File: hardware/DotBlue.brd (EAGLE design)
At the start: 24 x 24 mm, 11 parts, among them IC1 CP2101, J3 USB-MICROB, U1 RFD77101, X3 S4B-ZR

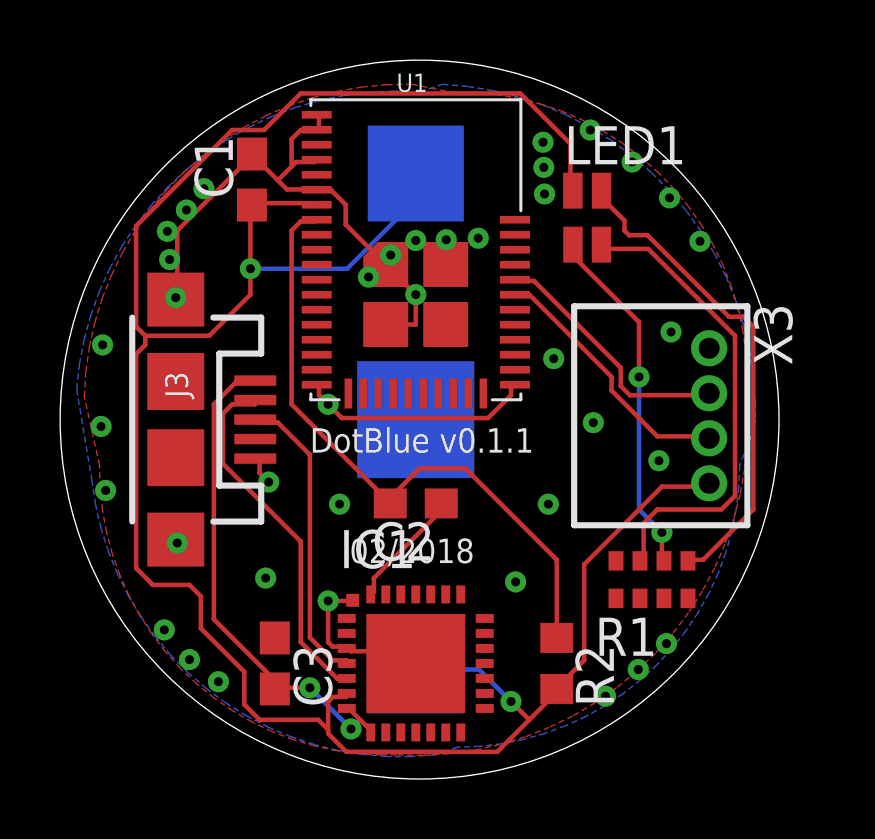
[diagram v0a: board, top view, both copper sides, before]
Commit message: Flip JST, add AIN
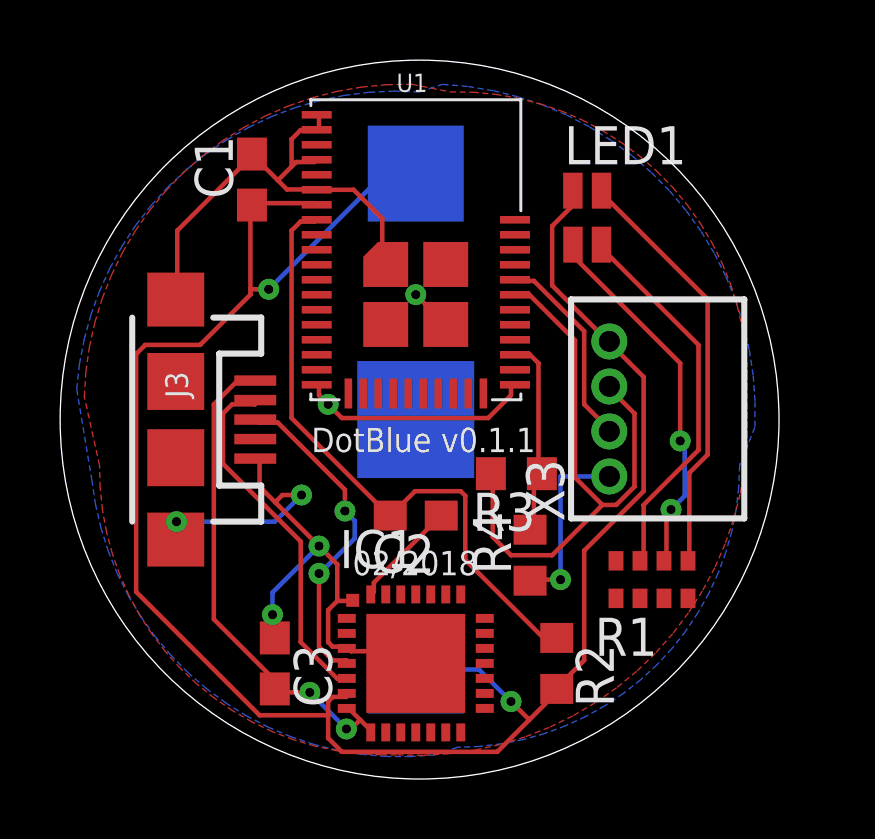
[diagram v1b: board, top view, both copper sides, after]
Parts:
- added R3, R4: (no value), rcl:R0603
- moved X3 3.34 mm to (21.6, 14.3), turned to 90 degrees
- moved C2 0.41 mm to (15.1, 10.8)
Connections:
- net OUTB renamed IO_B
- removed net OUTA: U1.36, X3.3
- new net AIN5: R3.1, R4.2, U1.32
- new net IO_A: R3.2, U1.36, X3.3
- net GND: now also R4.1
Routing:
- net IO_A: track 0.00 -> 20.2 mm
- net GND: track 34.5 -> 53.4 mm, vias 39 -> 7
- net +3V3: track 82.1 -> 67.6 mm
- net OUTA: track 8.73 -> 0.00 mm
- net AIN5: track 0.00 -> 6.75 mm
- net N$1: track 15.9 -> 12.7 mm
- net N$15: track 16.2 -> 14.1 mm
- net IO_B: track 8.46 -> 6.70 mm
- net USB_D+: track 10.0 -> 11.0 mm, vias 0 -> 2
- net N$4: track 11.8 -> 12.4 mm

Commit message: Swap IO_AB for I2C pins, correct traces near pins, solidify GND
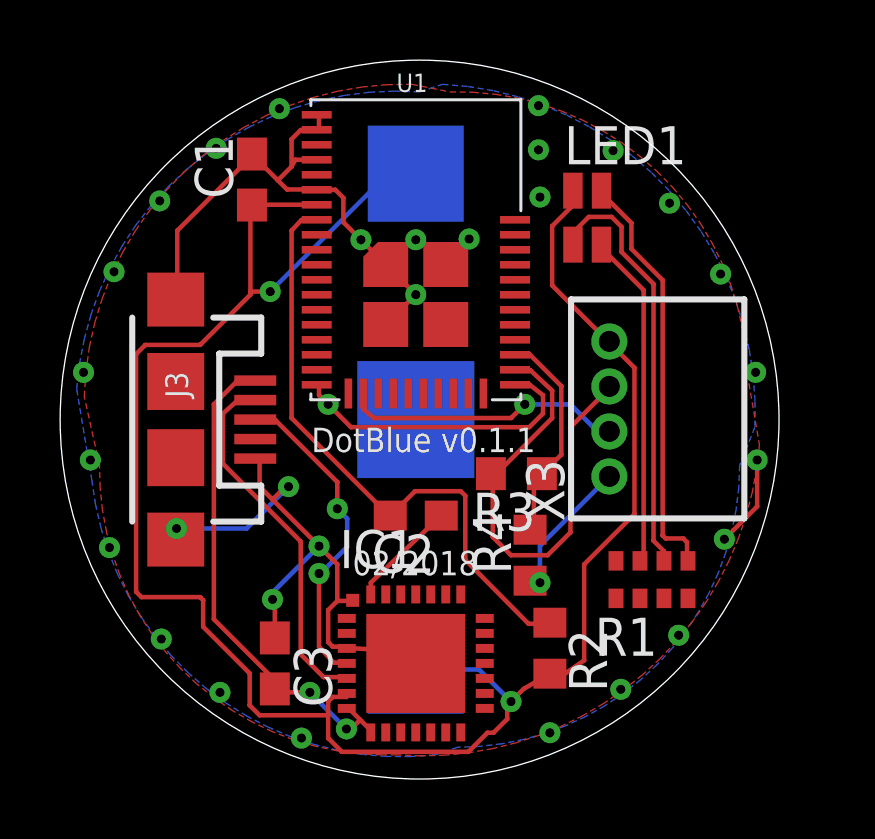
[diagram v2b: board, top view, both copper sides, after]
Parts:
- moved R2 0.56 mm to (19.6, 6.35)
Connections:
- removed net IO_A: R3.2, U1.36, X3.3
- removed net IO_B: U1.37, X3.2
- new net SCL: U1.21, X3.2
- new net SDA: R3.2, U1.31, X3.3
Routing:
- net IO_A: track 20.2 -> 0.00 mm
- net SDA: track 0.00 -> 16.1 mm
- net SCL: track 0.00 -> 9.42 mm, vias 0 -> 1
- net IO_B: track 6.70 -> 0.00 mm
- net GND: track 53.4 -> 58.4 mm, vias 7 -> 32
- net N$4: track 12.4 -> 14.2 mm, vias 2 -> 0
- net N$1: track 12.7 -> 11.2 mm

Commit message: Allign passive components
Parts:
- added BTN1: SPST.B3U-1000P(M), omron:B3U-1000P(M)
- moved C3 0.46 mm to (10.4, 6.30)
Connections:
- new net N$3: BTN1.1, U1.36
- net GND: now also BTN1.2
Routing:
- net N$3: track 0.00 -> 8.01 mm, vias 0 -> 1
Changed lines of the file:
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@@
 <layer number="20" name="Dimension" color="15" fill="1" visible="yes" active="yes"/>
 <layer number="21" name="tPlace" color="7" fill="1" visible="yes" active="yes"/>
-<layer number="22" name="bPlace" color="7" fill="1" visible="no" active="yes"/>
+<layer number="22" name="bPlace" color="7" fill="1" visible="yes" active="yes"/>
 <layer number="23" name="tOrigins" color="15" fill="1" visible="yes" active="yes"/>
-<layer number="24" name="bOrigins" color="15" fill="1" visible="no" active="yes"/>
+<layer number="24" name="bOrigins" color="15" fill="1" visible="yes" active="yes"/>
 <layer number="25" name="tNames" color="7" fill="1" visible="no" active="yes"/>
 <layer number="26" name="bNames" color="7" fill="1" visible="no" active="yes"/>
@@
 <text x="19.099096875" y="13.6985625" size="0.8128" layer="21" rot="R180">DotBlue v0.1.1</text>
 <text x="13.006503125" y="8.7804375" size="0.8128" layer="21">02/2018</text>
+<dimension x1="3.258853125" y1="13.957228125" x2="27.221146875" y2="13.982771875" x3="15.2146" y3="37.7952" textsize="1.778" layer="47" dtype="diameter"/>
 </plain>
 <attributes>
@@
 <element name="R2" library="rcl" package="R0603" value="" x="19.5834" y="6.35" rot="R270"/>
 <element name="U$1" library="adafruit" package="CR1220-SMD" value="" x="15.113" y="13.97" rot="MR270"/>
-<element name="C3" library="rcl" package="C0603" value="1uF" x="10.414" y="5.842" rot="R270"/>
+<element name="C3" library="rcl" package="C0603" value="1uF" x="10.4394" y="6.2992" rot="R270"/>
 <element name="R3" library="rcl" package="R0603" value="" x="18.4658" y="12.1666" rot="R180"/>
 <element name="R4" library="rcl" package="R0603" value="" x="18.923" y="9.4488" rot="R90"/>
+<element name="BTN1" library="omron" package="B3U-1000P(M)" value="SPST.B3U-1000P(M)" x="24.0284" y="14.2748" rot="MR270"/>
 </elements>
 <signals>
@@
 <wire x1="10.8712" y1="11.7348" x2="10.7696" y2="11.7348" width="0.1524" layer="1"/>
 <wire x1="10.7696" y1="11.7348" x2="10.3378" y2="11.303" width="0.1524" layer="1"/>
-<wire x1="10.414" y1="6.692" x2="10.414" y2="7.8994" width="0.1524" layer="1"/>
+<wire x1="10.4394" y1="7.1492" x2="10.414" y2="7.8994" width="0.1524" layer="1"/>
 <wire x1="10.414" y1="7.8994" x2="10.3378" y2="7.9756" width="0.1524" layer="1"/>
 <via x="10.3378" y="7.9756" extent="1-16" drill="0.3"/>
@@
 <via x="15.113" y="19.9644" extent="1-16" drill="0.3"/>
 <via x="13.2842" y="19.9644" extent="1-16" drill="0.3"/>
+<contactref element="BTN1" pad="2"/>
 </signal>
 <signal name="+5V">
@@
 <wire x1="9.144" y1="15.24" x2="8.382" y2="14.478" width="0.1524" layer="1"/>
 <wire x1="9.7536" y1="15.24" x2="9.144" y2="15.24" width="0.1524" layer="1"/>
-<wire x1="10.3632" y1="5.0292" x2="10.414" y2="4.992" width="0.1524" layer="1"/>
+<wire x1="10.3632" y1="5.0292" x2="10.4394" y2="5.4492" width="0.1524" layer="1"/>
 <wire x1="9.7536" y1="15.24" x2="9.762" y2="15.27" width="0.1524" layer="1"/>
 <wire x1="12.954" y1="3.6576" x2="13.2588" y2="3.9624" width="0.1524" layer="1"/>
 <wire x1="12.8016" y1="3.6576" x2="12.954" y2="3.6576" width="0.1524" layer="1"/>
 <wire x1="11.5824" y1="4.8768" x2="12.8016" y2="3.6576" width="0.1524" layer="16"/>
-<wire x1="10.5156" y1="4.8768" x2="11.5824" y2="4.8768" width="0.1524" layer="1"/>
-<wire x1="10.5156" y1="4.8768" x2="10.414" y2="4.992" width="0.1524" layer="1"/>
+<wire x1="10.5156" y1="5.3086" x2="11.5824" y2="4.8768" width="0.1524" layer="1"/>
+<wire x1="10.5156" y1="5.3086" x2="10.4394" y2="5.4492" width="0.1524" layer="1"/>
 <via x="12.8016" y="3.6576" extent="1-16" drill="0.3"/>
 <via x="11.5824" y="4.8768" extent="1-16" drill="0.3"/>
@@
 <via x="18.7452" y="14.478" extent="1-16" drill="0.3"/>
 </signal>
+<signal name="N$3">
+<contactref element="BTN1" pad="1"/>
+<contactref element="U1" pad="36"/>
+<wire x1="18.421" y1="18.13" x2="19.1572" y2="18.13" width="0.1524" layer="1"/>
+<wire x1="19.1572" y1="18.13" x2="19.7866" y2="17.5006" width="0.1524" layer="1"/>
+<wire x1="19.7866" y1="17.5006" x2="19.7866" y2="16.7132" width="0.1524" layer="1"/>
+<wire x1="19.7866" y1="16.7132" x2="19.685" y2="16.6116" width="0.1524" layer="1"/>
+<via x="19.685" y="16.6116" extent="1-16" drill="0.3"/>
+<wire x1="19.685" y1="16.6116" x2="19.7104" y2="16.6116" width="0.1524" layer="16"/>
+<wire x1="19.7104" y1="16.6116" x2="20.7518" y2="17.653" width="0.1524" layer="16"/>
+<wire x1="20.7518" y1="17.653" x2="22.4002" y2="17.653" width="0.1524" layer="16"/>
+<wire x1="22.4002" y1="17.653" x2="24.0284" y2="16.0248" width="0.1524" layer="16"/>
+</signal>
 </signals>

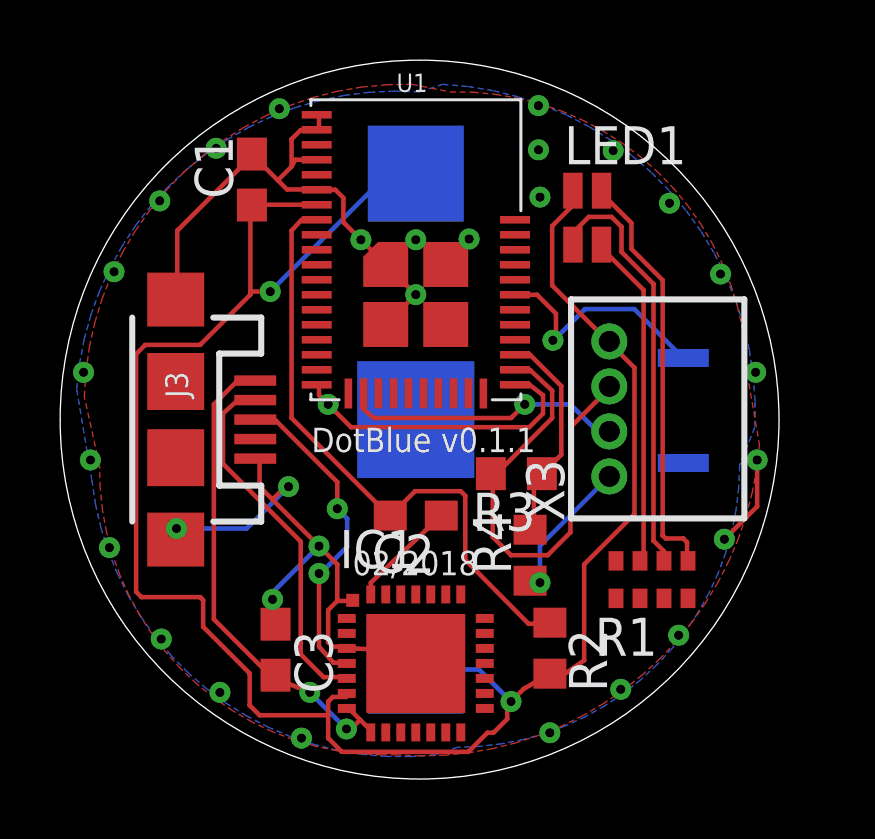
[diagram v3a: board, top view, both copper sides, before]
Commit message: Add 3-way JMP for 3V-5V switch of JST
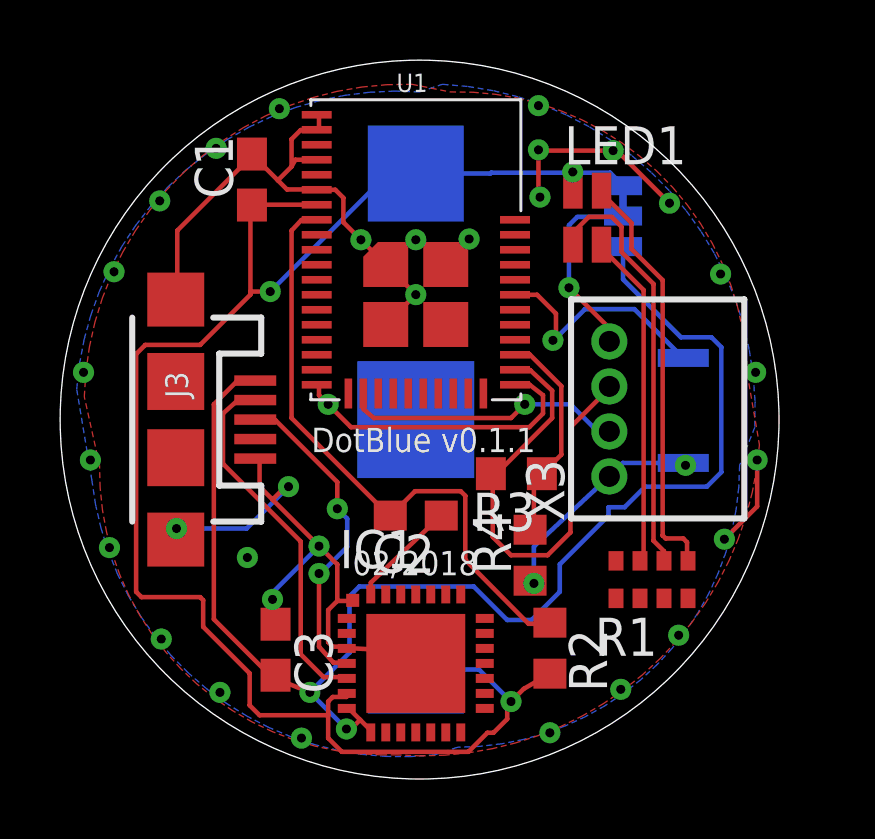
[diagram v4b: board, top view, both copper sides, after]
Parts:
- added JP1: JUMPER-SMT_3_1-NC_TRACE_NO-SILK, SparkFun-Jumpers:SMT-JUMPER_3_1-NC_TRACE_NO-SILK
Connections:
- new net N$5: JP1.2, X3.4
- net +3V3: now also JP1.3; no longer X3.4
- net +5V: now also JP1.1
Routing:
- net +5V: track 17.2 -> 46.2 mm
- net +3V3: track 68.1 -> 56.8 mm, vias 2 -> 3
- net GND: track 58.0 -> 67.7 mm, vias 32 -> 34
- net N$5: track 0.00 -> 6.36 mm, vias 0 -> 1
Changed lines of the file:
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@@
 <layer number="45" name="Holes" color="7" fill="1" visible="no" active="yes"/>
 <layer number="46" name="Milling" color="3" fill="1" visible="no" active="yes"/>
-<layer number="47" name="Measures" color="7" fill="1" visible="no" active="yes"/>
+<layer number="47" name="Measures" color="7" fill="1" visible="yes" active="yes"/>
 <layer number="48" name="Document" color="7" fill="1" visible="no" active="yes"/>
 <layer number="49" name="Reference" color="7" fill="1" visible="no" active="yes"/>
@@
 <element name="R4" library="rcl" package="R0603" value="" x="18.923" y="9.4488" rot="R90"/>
 <element name="BTN1" library="omron" package="B3U-1000P(M)" value="SPST.B3U-1000P(M)" x="24.0284" y="14.2748" rot="MR270"/>
+<element name="JP1" library="SparkFun-Jumpers" package="SMT-JUMPER_3_1-NC_TRACE_NO-SILK" value="JUMPER-SMT_3_1-NC_TRACE_NO-SILK" x="22.0218" y="20.7518" rot="MR90"/>
 </elements>
 <signals>
@@
 <via x="15.113" y="18.1356" extent="1-16" drill="0.3"/>
 <wire x1="18.923" y1="8.5988" x2="19.1888" y2="8.5988" width="0.1524" layer="1"/>
-<wire x1="19.1888" y1="8.5988" x2="19.2532" y2="8.5344" width="0.1524" layer="1"/>
-<via x="19.2532" y="8.5344" extent="1-16" drill="0.3"/>
-<wire x1="19.2532" y1="8.5344" x2="19.2532" y2="9.7642" width="0.1524" layer="16"/>
-<wire x1="19.2532" y1="9.7642" x2="21.5646" y2="12.0756" width="0.1524" layer="16"/>
+<wire x1="19.1888" y1="8.5988" x2="19.05" y2="8.509" width="0.1524" layer="1"/>
+<via x="19.05" y="8.509" extent="1-16" drill="0.3"/>
+<wire x1="19.05" y1="8.509" x2="19.05" y2="9.7388" width="0.1524" layer="16"/>
+<wire x1="19.05" y1="9.7388" x2="21.5646" y2="12.0756" width="0.1524" layer="16"/>
 <wire x1="11.811" y1="21.63" x2="12.4314" y2="21.63" width="0.1524" layer="1"/>
 <wire x1="12.4314" y1="21.63" x2="12.7" y2="21.3614" width="0.1524" layer="1"/>
@@
 <via x="13.2842" y="19.9644" extent="1-16" drill="0.3"/>
 <contactref element="BTN1" pad="2"/>
+<wire x1="26.3932" y1="12.5248" x2="26.4922" y2="12.6238" width="0.1524" layer="16"/>
+<wire x1="24.0284" y1="12.5248" x2="22.0138" y2="12.5248" width="0.1524" layer="16"/>
+<wire x1="22.0138" y1="12.5248" x2="21.5646" y2="12.0756" width="0.1524" layer="16"/>
+<wire x1="21.6916" y1="22.9362" x2="21.8186" y2="22.9362" width="0.1524" layer="1"/>
+<wire x1="21.8186" y1="22.9362" x2="23.5712" y2="21.1836" width="0.1524" layer="1"/>
+<wire x1="21.6916" y1="22.9362" x2="19.2278" y2="22.9362" width="0.1524" layer="1"/>
+<wire x1="19.2278" y1="22.9362" x2="19.2024" y2="22.9616" width="0.1524" layer="1"/>
+<wire x1="19.2024" y1="22.9616" x2="19.2024" y2="21.4376" width="0.1524" layer="1"/>
+<wire x1="19.2024" y1="21.4376" x2="19.2532" y2="21.3868" width="0.1524" layer="1"/>
+<via x="9.4996" y="9.3726" extent="1-16" drill="0.3"/>
+<via x="24.1046" y="12.446" extent="1-16" drill="0.3"/>
+<wire x1="24.1046" y1="12.446" x2="24.0284" y2="12.5248" width="0" layer="19" extent="16-16"/>
 </signal>
 <signal name="+5V">
@@
 <via x="12.8016" y="3.6576" extent="1-16" drill="0.3"/>
 <via x="11.5824" y="4.8768" extent="1-16" drill="0.3"/>
+<contactref element="JP1" pad="1"/>
+<wire x1="22.0218" y1="19.7358" x2="22.0218" y2="18.6436" width="0.1524" layer="16"/>
+<wire x1="22.0218" y1="18.6436" x2="23.9522" y2="16.7132" width="0.1524" layer="16"/>
+<wire x1="23.9522" y1="16.7132" x2="24.9682" y2="16.7132" width="0.1524" layer="16"/>
+<wire x1="24.9682" y1="16.7132" x2="25.2984" y2="16.383" width="0.1524" layer="16"/>
+<wire x1="25.2984" y1="16.383" x2="25.2984" y2="12.2174" width="0.1524" layer="16"/>
+<wire x1="25.2984" y1="12.2174" x2="24.8158" y2="11.7348" width="0.1524" layer="16"/>
+<wire x1="24.8158" y1="11.7348" x2="22.7584" y2="11.7348" width="0.1524" layer="16"/>
+<wire x1="22.7584" y1="11.7348" x2="22.0726" y2="11.049" width="0.1524" layer="16"/>
+<wire x1="22.0726" y1="11.049" x2="21.5392" y2="11.049" width="0.1524" layer="16"/>
+<wire x1="21.5392" y1="11.049" x2="21.5392" y2="10.7696" width="0.1524" layer="16"/>
+<wire x1="21.5392" y1="10.7696" x2="19.9136" y2="9.144" width="0.1524" layer="16"/>
+<wire x1="19.9136" y1="9.144" x2="19.9136" y2="8.2296" width="0.1524" layer="16"/>
+<wire x1="19.9136" y1="8.2296" x2="18.9738" y2="7.2898" width="0.1524" layer="16"/>
+<wire x1="18.9738" y1="7.2898" x2="18.161" y2="7.2898" width="0.1524" layer="16"/>
+<wire x1="18.161" y1="7.2898" x2="17.0434" y2="8.4074" width="0.1524" layer="16"/>
+<wire x1="17.0434" y1="8.4074" x2="13.2334" y2="8.4074" width="0.1524" layer="16"/>
+<wire x1="11.5316" y1="4.9276" x2="11.5824" y2="4.8768" width="0.1524" layer="16"/>
+<wire x1="13.2334" y1="8.4074" x2="12.9032" y2="8.0772" width="0.1524" layer="16"/>
+<wire x1="12.9032" y1="8.0772" x2="12.9032" y2="6.1976" width="0.1524" layer="16"/>
+<wire x1="12.9032" y1="6.1976" x2="11.5824" y2="4.8768" width="0.1524" layer="16"/>
 </signal>
 <signal name="USB_D-">
@@
 <contactref element="IC1" pad="6"/>
 <contactref element="U1" pad="7"/>
-<contactref element="X3" pad="4"/>
 <contactref element="C1" pad="1"/>
 <contactref element="R2" pad="2"/>
 <contactref element="U$1" pad="+$1"/>
 <contactref element="U$1" pad="+$2"/>
-<wire x1="20.2692" y1="21.0312" x2="20.2692" y2="21.4884" width="0.1524" layer="1"/>
-<wire x1="19.6596" y1="20.4216" x2="20.2692" y2="21.0312" width="0.1524" layer="1"/>
-<wire x1="19.6596" y1="18.4404" x2="19.6596" y2="20.4216" width="0.1524" layer="1"/>
-<wire x1="21.4884" y1="16.6116" x2="19.6596" y2="18.4404" width="0.1524" layer="1"/>
-<wire x1="20.2692" y1="21.4884" x2="20.3505" y2="21.601" width="0.1524" layer="1"/>
-<wire x1="21.4884" y1="16.6116" x2="21.5646" y2="16.5756" width="0.1524" layer="1"/>
 <wire x1="9.6774" y1="21.1328" x2="11.684" y2="21.1328" width="0.1524" layer="1"/>
 <wire x1="11.684" y1="21.1328" x2="11.811" y2="21.13" width="0.1524" layer="1"/>
@@
 <wire x1="18.288" y1="4.572" x2="17.2212" y2="5.6388" width="0.1524" layer="16"/>
 <wire x1="15.24" y1="5.6388" x2="15.113" y2="5.77" width="0.1524" layer="16"/>
-<wire x1="22.4028" y1="15.6972" x2="21.6408" y2="16.4592" width="0.1524" layer="1"/>
-<wire x1="22.4028" y1="10.8204" x2="22.4028" y2="15.6972" width="0.1524" layer="1"/>
-<wire x1="20.7264" y1="9.144" x2="22.4028" y2="10.8204" width="0.1524" layer="1"/>
-<wire x1="20.7264" y1="5.9436" x2="20.7264" y2="9.144" width="0.1524" layer="1"/>
-<wire x1="19.812" y1="5.3086" x2="20.7264" y2="5.9436" width="0.1524" layer="1"/>
-<wire x1="21.6408" y1="16.4592" x2="21.5646" y2="16.5756" width="0.1524" layer="1"/>
-<wire x1="19.812" y1="5.3086" x2="19.5834" y2="5.5" width="0.1524" layer="1"/>
 <via x="18.288" y="4.572" extent="1-16" drill="0.3"/>
 <wire x1="15.113" y1="22.17" x2="14.1944" y2="22.17" width="0.1524" layer="16"/>
@@
 <wire x1="18.288" y1="4.572" x2="18.708" y2="4.992" width="0.1524" layer="1"/>
 <wire x1="18.708" y1="4.992" x2="19.5834" y2="5.5" width="0.1524" layer="1"/>
+<contactref element="JP1" pad="3"/>
+<wire x1="15.113" y1="22.17" x2="17.598" y2="22.17" width="0.1524" layer="16"/>
+<wire x1="17.598" y1="22.17" x2="17.6276" y2="22.1996" width="0.1524" layer="16"/>
+<wire x1="17.6276" y1="22.1996" x2="20.3708" y2="22.1996" width="0.1524" layer="16"/>
+<wire x1="20.3708" y1="22.1996" x2="21.59" y2="22.1996" width="0.1524" layer="16"/>
+<wire x1="21.59" y1="22.1996" x2="22.0218" y2="21.7678" width="0.1524" layer="16"/>
+<wire x1="20.3505" y1="21.601" x2="20.3251" y2="22.2707" width="0.1524" layer="1"/>
+<wire x1="20.3251" y1="22.2707" x2="20.3454" y2="22.225" width="0.1524" layer="1"/>
+<via x="20.3454" y="22.225" extent="1-16" drill="0.3"/>
+<wire x1="20.3454" y1="22.225" x2="20.32" y2="22.2504" width="0.1524" layer="16"/>
+<wire x1="20.3454" y1="22.225" x2="20.3708" y2="22.1996" width="0.1524" layer="16"/>
 </signal>
 <signal name="LED_GREEN">
@@
 <wire x1="22.4002" y1="17.653" x2="24.0284" y2="16.0248" width="0.1524" layer="16"/>
 </signal>
+<signal name="N$5">
+<contactref element="X3" pad="4"/>
+<contactref element="JP1" pad="2"/>
+<wire x1="21.5646" y1="16.5756" x2="21.5646" y2="17.018" width="0.1524" layer="1"/>
+<wire x1="21.5646" y1="17.018" x2="20.2184" y2="18.3642" width="0.1524" layer="1"/>
+<via x="20.2184" y="18.3642" extent="1-16" drill="0.3"/>
+<wire x1="20.2184" y1="18.3642" x2="20.2184" y2="20.447" width="0.1524" layer="16"/>
+<wire x1="20.2184" y1="20.447" x2="20.4978" y2="20.7264" width="0.1524" layer="16"/>
+<wire x1="20.4978" y1="20.7264" x2="21.9964" y2="20.7264" width="0.1524" layer="16"/>
+<wire x1="21.9964" y1="20.7264" x2="22.0218" y2="20.7518" width="0.1524" layer="16"/>
+</signal>
 </signals>
